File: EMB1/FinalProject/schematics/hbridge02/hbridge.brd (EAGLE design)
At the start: 119.4 x 96.5 mm, 36 parts, among them K1 61201021621, Q10 IRF512, Q3 IRF512, Q4 IRF512, Q5 IRF512, Q6 IRF512, Q7 IRF512, Q8 IRF512, Q9 IRF512

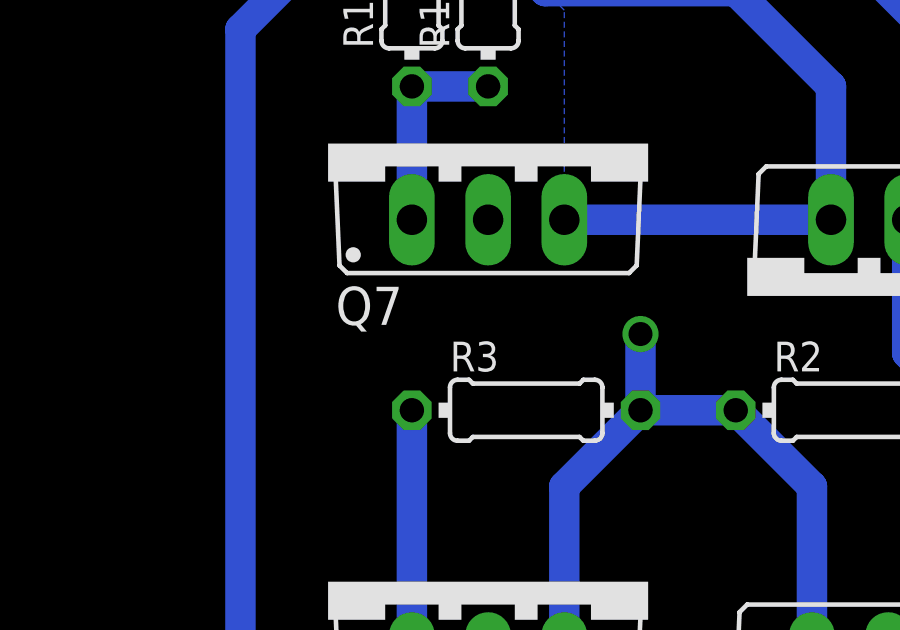
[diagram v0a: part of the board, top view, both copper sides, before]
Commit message: code updated: made 16 bit and PID fixed to give good results
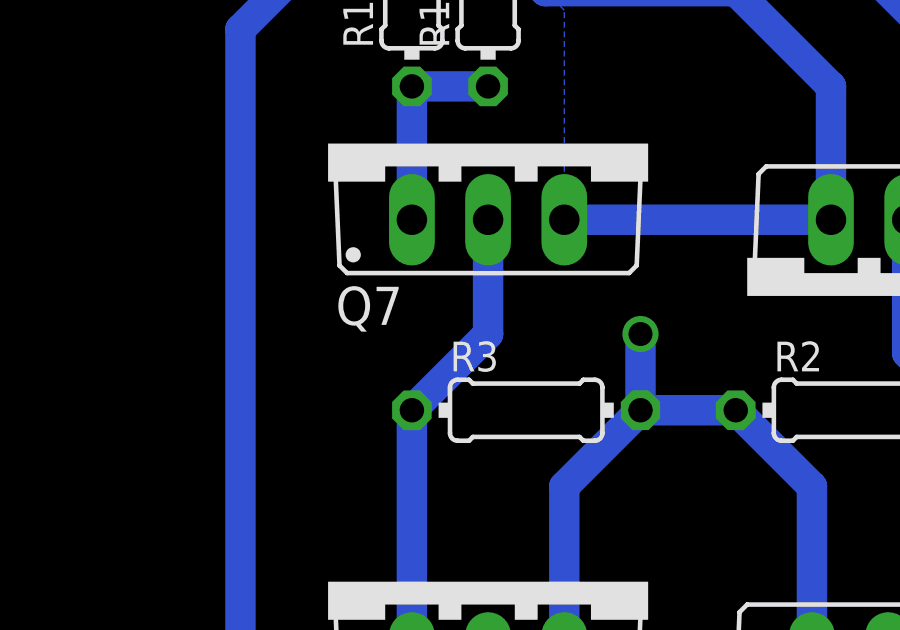
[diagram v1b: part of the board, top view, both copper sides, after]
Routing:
- net N$12: track 8.26 -> 15.7 mm
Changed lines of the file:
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@@
 <contactref element="R3" pad="1"/>
 <wire x1="6.35" y1="54.61" x2="6.35" y2="62.865" width="1.016" layer="16"/>
-<wire x1="6.35" y1="62.865" x2="8.89" y2="69.215" width="0" layer="19" extent="1-1"/>
+<wire x1="6.35" y1="62.865" x2="8.89" y2="65.405" width="1.016" layer="16"/>
+<wire x1="8.89" y1="65.405" x2="8.89" y2="69.215" width="1.016" layer="16"/>
 </signal>
 <signal name="N$10">
